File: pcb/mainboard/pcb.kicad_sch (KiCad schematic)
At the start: 0 parts

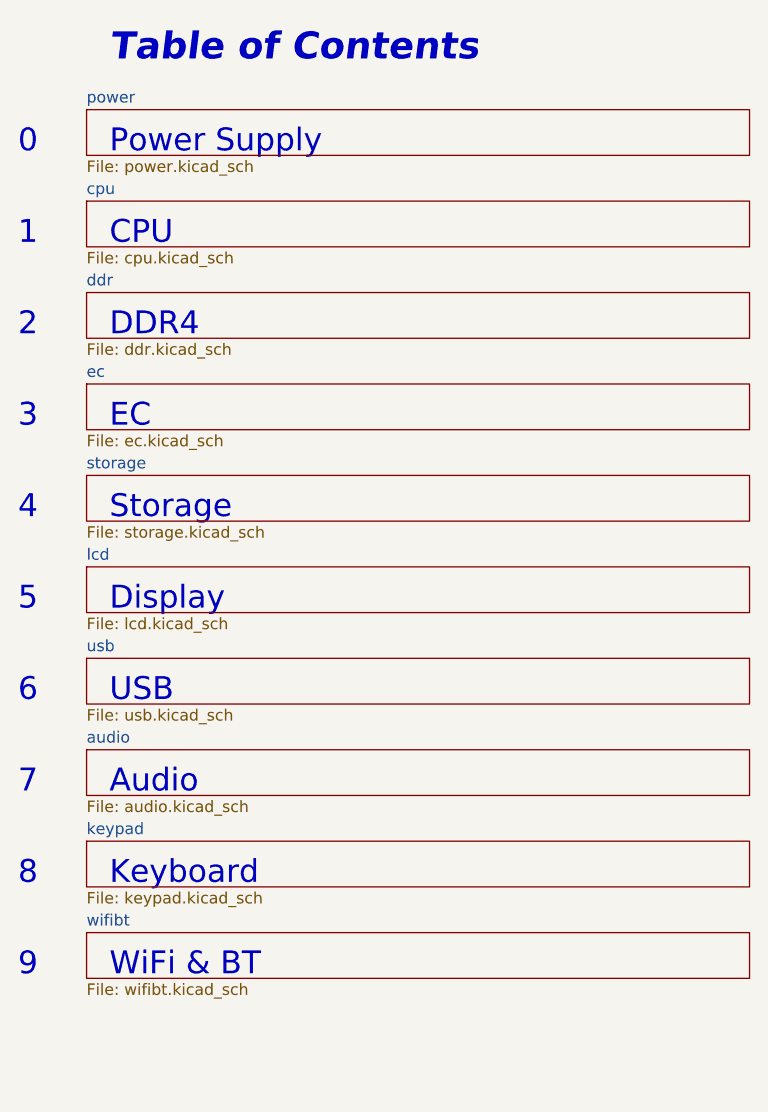
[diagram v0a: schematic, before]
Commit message: pcb: preliminary r0p1 schematics
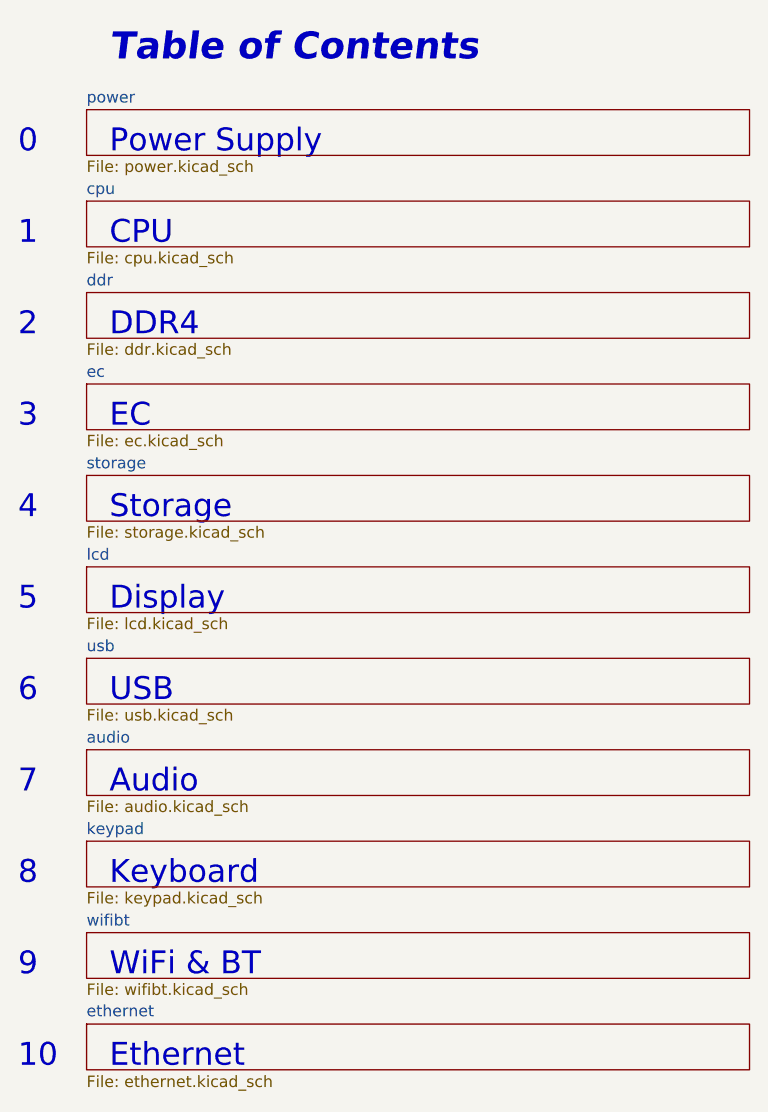
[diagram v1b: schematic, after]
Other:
- added sheet ethernet (ethernet.kicad_sch)
- note added: "10"
- note added: "Ethernet"
- company: Copyright EI-2030 2021. / Engineer: Wenting Zhang -> Copyright Modos 2021. / Engineer: Wenting Zhang
